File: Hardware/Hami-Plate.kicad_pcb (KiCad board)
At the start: 2 copper layers, 79.5 x 119.1 mm, 22 parts, among them SW10 MX, SW11 MX, SW12 MX, SW13 MX, SW14 MX, SW15 MX, SW16 MX, SW17 MX, SW18 MX, SW19 MX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

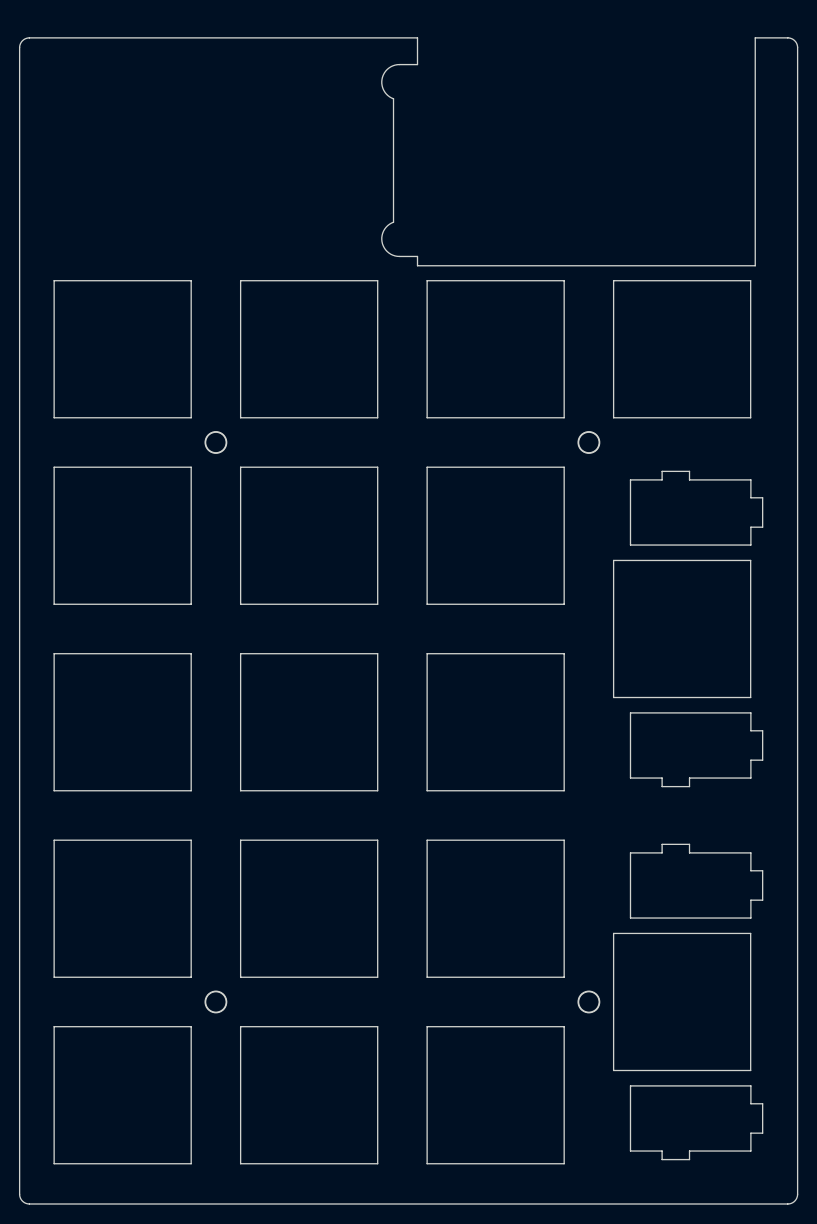
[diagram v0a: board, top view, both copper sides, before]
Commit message: Moved position of OLED, added new plate
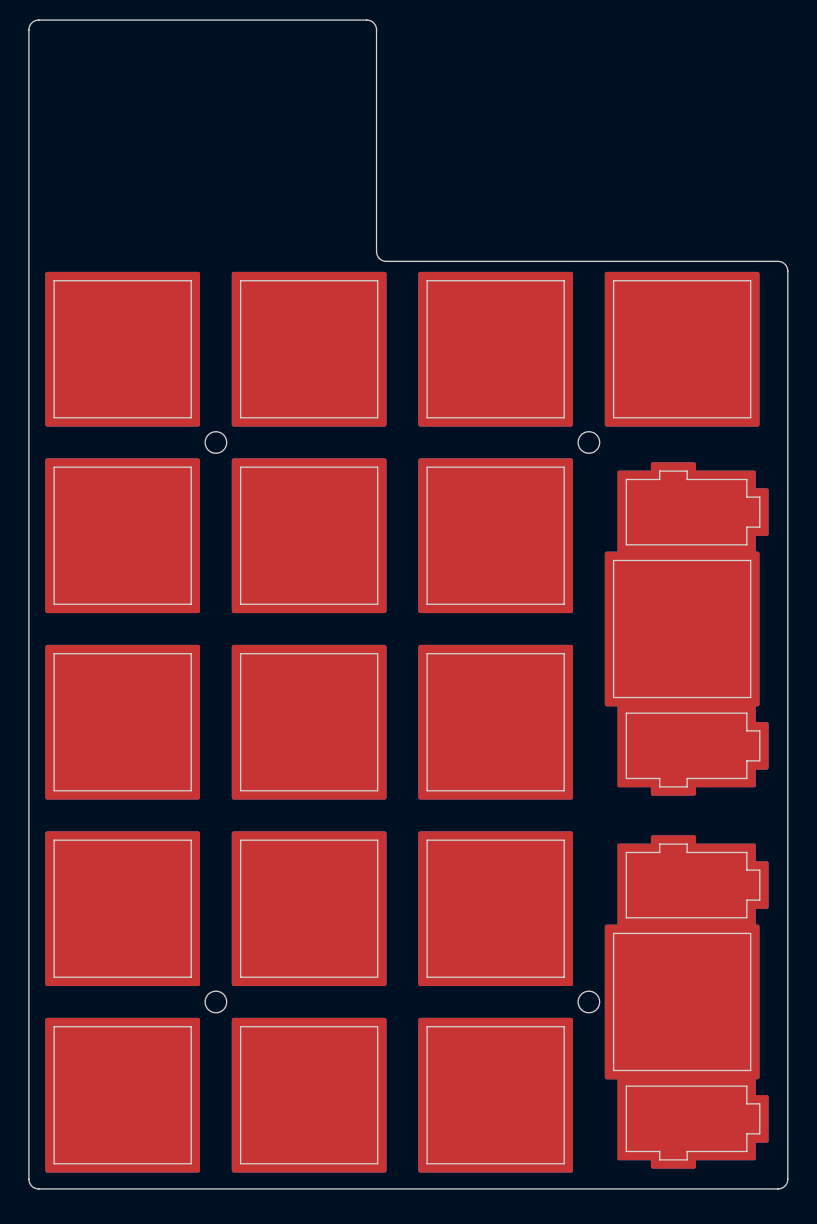
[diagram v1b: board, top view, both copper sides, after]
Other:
- board size 79.5 x 119.1 mm -> 77.5 x 119.4 mm
